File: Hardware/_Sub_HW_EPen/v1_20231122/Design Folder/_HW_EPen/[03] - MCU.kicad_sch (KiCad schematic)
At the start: 8 parts, among them U301 PIC16F15223_8BIT

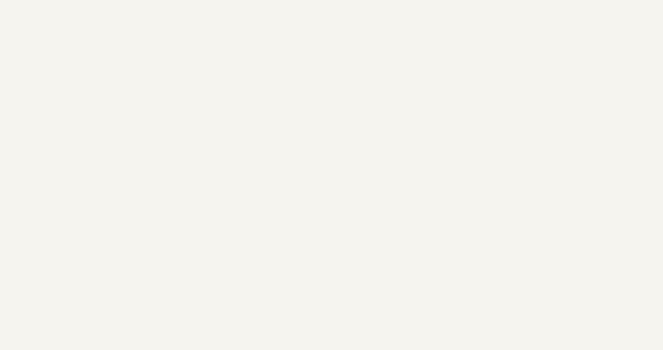
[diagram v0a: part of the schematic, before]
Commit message: Working on EPen schematic
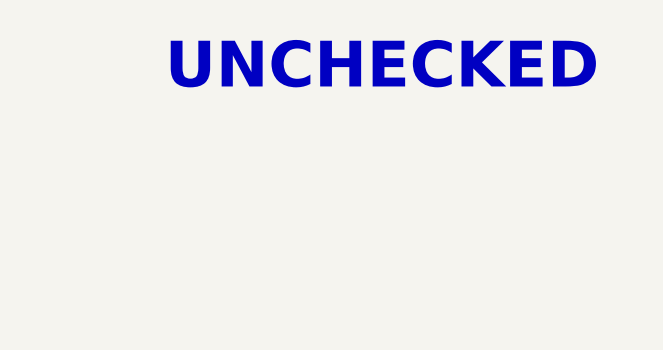
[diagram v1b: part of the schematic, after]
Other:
- note added: "UNCHECKED"
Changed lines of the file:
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@@
     (effects (font (size 1.27 1.27)) (justify left bottom))
+  )
+  (text "UNCHECKED" (at 369.57 36.83 0)
+    (effects (font (size 5.08 5.08) (thickness 1.016) bold) (justify left bottom))
   )
   (label "PIC_~{MCLR}" (at 170.18 115.57 0) (fields_autoplaced)

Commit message: Working on Epen Schematic
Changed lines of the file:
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@@
     (effects (font (size 1.27 1.27)) (justify left bottom))
   )
-  (hierarchical_label "SPI_MOSI" (shape output) (at 231.14 132.08 0) (fields_autoplaced)
+  (hierarchical_label "SPI_MOSI" (shape output) (at 231.14 129.54 0) (fields_autoplaced)
     (effects (font (size 1.27 1.27)) (justify left))
   )
@@
     (effects (font (size 1.27 1.27)) (justify right))
   )
+  (hierarchical_label "SPI_MISO" (shape input) (at 231.14 132.08 0) (fields_autoplaced)
+    (effects (font (size 1.27 1.27)) (justify left))
+  )
   (hierarchical_label "SPI_CS" (shape output) (at 231.14 134.62 0) (fields_autoplaced)
     (effects (font (size 1.27 1.27)) (justify left))
   )
-  (hierarchical_label "MIC5365_EN" (shape output) (at 231.14 127 0) (fields_autoplaced)
+  (hierarchical_label "MIC5365_EN" (shape output) (at 231.14 124.46 0) (fields_autoplaced)
     (effects (font (size 1.27 1.27)) (justify left))
   )
@@
     (effects (font (size 1.27 1.27)) (justify left))
   )
-  (hierarchical_label "SPI_CLK" (shape output) (at 231.14 129.54 0) (fields_autoplaced)
+  (hierarchical_label "SPI_CLK" (shape output) (at 231.14 127 0) (fields_autoplaced)
     (effects (font (size 1.27 1.27)) (justify left))
   )

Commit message: More progress on EPen Hardware
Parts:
- added R304: 27R_1/16W_1%, Resistor_SMD:R_0402_1005Metric, symbol _SCHLIB_EPen:RES_27R_1/16W_1%_R0402
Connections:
- net IND_LED: now also U301.2 (RA5); no longer U301.5 (RC5)
- net MIC5365_EN: now also U301.3 (RA4)
- net SPI_CLK: now also U301.10 (RC0)
- net SPI_CS: now also U301.7 (RC3)
- net SPI_MISO: now also R304.1
- net SPI_MOSI: now also U301.8 (RC2)
- net MCU_~{RESET}: now reaches U301.11 (RA2)
- net EEPROM_~{WP}: now reaches U301.12 (ICSPCLK/RA1)
- net BUFF_~{EN}: now reaches U301.13 (ICSPDAT/RA0)
- net UART_TX: now reaches U301.6 (RC4)
- net at U301.9 (RC1): now also R304.2
- new net UART_RX: U301.5 (RC5)
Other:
- note removed: "UNCHECKED"
- company: (none) -> mend0z0

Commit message: _HW_EPen is ready to be worked for layout
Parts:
- removed R303: 100R_1/10W_1%, Resistor_SMD:R_0402_1005Metric, symbol _SCHLIB_EPen:RES_100R_1/10W_1%_R0402
- added J301: HDR_4POS_VERT, Connector_PinHeader_2.54mm:PinHeader_1x04_P2.54mm_Vertical, symbol _SCHLIB_EPen:CONN_HEADER_4POS_1ROW_VERT_2.54mm
- added R303: 470R_1/16W_1%, Resistor_SMD:R_0402_1005Metric, symbol _SCHLIB_EPen:RES_470R_1/16W_1%_R0402
- C301, C302, C303, LED301, R301, R302, R304: SCH CHECK SCH (N/A) -> SCH (CHECKED)
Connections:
- net BUFF_~{EN}: now also J301.3
- net EEPROM_~{WP}: now also J301.4
- net GND: now also J301.2
- net IND_LED: now also R303.1
- net PIC_~{MCLR}: now also J301.1
- net at LED301.2: now also R303.2
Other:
- note added: "CIRCUITS"
- note added: "CRYSTAL CIRCUIT"
- note added: "DONE"
- note added: "I = 5mA @ 5V"
- note added: "NO_EXT CIRCUIT"
- note added: "POWER SUPPLY"
- note added: "PROGRAMMER PINS"
- note added: "PROGRAMMING CIRCUIT"
- note added: "RESET CIRCUIT"
- note added: "STATUS"
- note removed: "I = 5mA @ 3.3V"
- title: (none) -> _HW_EPen

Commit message: Updating file templates and structures...
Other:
- moved on the sheet: C301, C302, C303, J301, LED301, R301, R302, R303, R304, U301

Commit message: Updating Hardware File structures
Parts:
- C301, C303: Manufacturer (none) -> Murata Electronics; Part Number GRM155R71H104KE14J -> (none); Part Number (Manufacturer) (none) -> GRM155R71H104KE14J; Part Number (Vendor) (none) -> 490-13342-2-ND; Vendor (none) -> Digikey
- C302: Manufacturer (none) -> Murata Electronics; Part Number GRM155Z71A105KE01D -> (none); Part Number (Manufacturer) (none) -> GRM155Z71A105KE01D; Part Number (Vendor) (none) -> 490-GRM155Z71A105KE01DTR-ND; Vendor (none) -> Digikey
- J301: Manufacturer (none) -> Adam Tech; Part Number PH1-04-UA -> (none); Part Number (Manufacturer) (none) -> PH1-04-UA; Part Number (Vendor) (none) -> 2057-PH1-04-UA-ND; Vendor (none) -> Digikey
- LED301: Manufacturer (none) -> Harvatek Corporation; Part Number B2841NG--05D000514U1930 -> (none); Part Number (Manufacturer) (none) -> B2841NG--05D000514U1930; Part Number (Vendor) (none) -> 3147-B2841NG--05D000514U1930TR-ND; Vendor (none) -> Digikey
- R301: Manufacturer (none) -> Bourns Inc.; Part Number CR0402-FX-1002GLF -> (none); Part Number (Manufacturer) (none) -> CR0402-FX-1002GLF; Part Number (Vendor) (none) -> CR0402-FX-1002GLFTR-ND; Vendor (none) -> Digikey
- R302: Manufacturer (none) -> Stackpole Electronics Inc; Part Number RNCP0805FTD1R00 -> (none); Part Number (Manufacturer) (none) -> RNCP0805FTD1R00; Part Number (Vendor) (none) -> RNCP0805FTD1R00TR-ND; Vendor (none) -> Digikey
- R303: Manufacturer (none) -> Bourns Inc.; Part Number CR0402-FX-4700GLF -> (none); Part Number (Manufacturer) (none) -> CR0402-FX-4700GLF; Part Number (Vendor) (none) -> CR0402-FX-4700GLFTR-ND; Vendor (none) -> Digikey
- R304: Manufacturer (none) -> Bourns Inc.; Part Number CR0402-FX-27R0GLF -> (none); Part Number (Manufacturer) (none) -> CR0402-FX-27R0GLF; Part Number (Vendor) (none) -> CR0402-FX-27R0GLFTR-ND; Vendor (none) -> Digikey
- U301: Manufacturer (none) -> Microchip Technology; Part Number PIC16F15223-E/SL -> (none); Part Number (Manufacturer) (none) -> PIC16F15223-E/SL; Part Number (Vendor) (none) -> 150-PIC16F15223-E/SL-ND; Vendor (none) -> Digikey
